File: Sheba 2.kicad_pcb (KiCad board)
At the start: 2 copper layers, 85.7 x 54 mm, 69 parts, among them J1 Conn_01x02_Pin, J2 Conn_02x04_Top_Bottom, J3 Conn_01x06_Pin, J4 Conn_01x03_Pin, J5 Conn_01x03_Pin, J6 Conn_01x03_Pin, P1 USB 2.0 Type-C Port, SW1 SPDT Switch, U1 STM32F072CBTx, U2 MIC5504-3.3YM5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

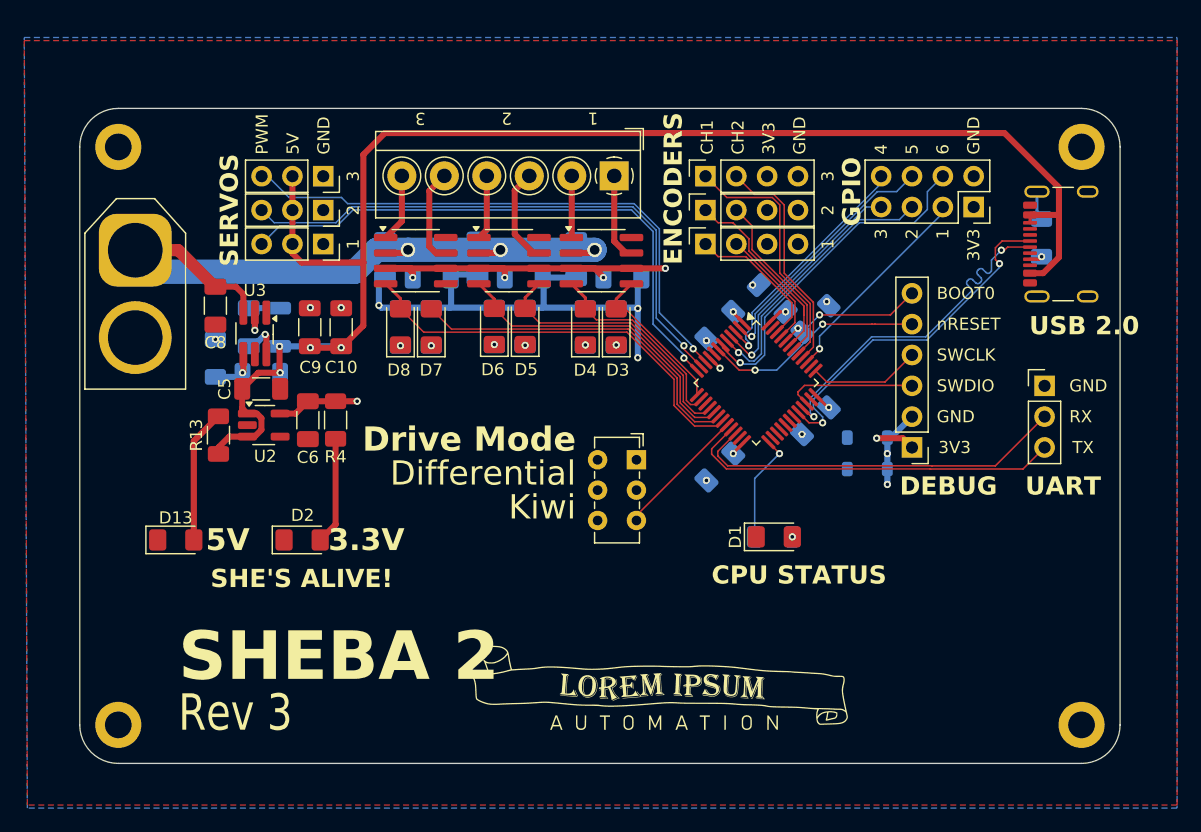
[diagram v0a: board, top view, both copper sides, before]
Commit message: change to ESP32-C6-WROOM
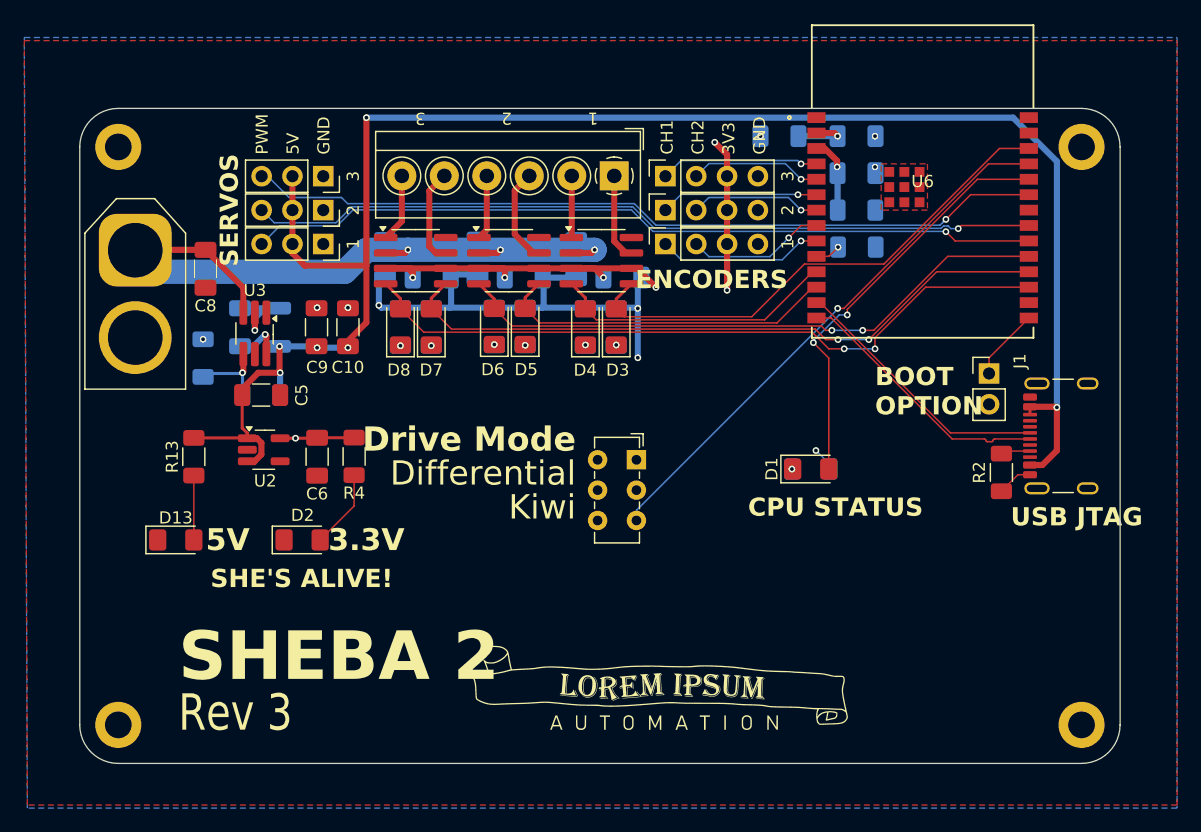
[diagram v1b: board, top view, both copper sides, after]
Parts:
- removed C4: C1uF, Capacitor_SMD:C_1206_3216Metric_Pad1.33x1.80mm_HandSolder
- removed D10, D9: D_Zener3.3V, Diode_SMD:D_SOD-123
- removed J2: Conn_02x04_Top_Bottom, Connector_PinSocket_2.54mm:PinSocket_2x04_P2.54mm_Vertical
- removed J3: Conn_01x06_Pin, Connector_PinHeader_2.54mm:PinHeader_1x06_P2.54mm_Vertical
- removed U1: STM32F072CBTx, Package_QFP:LQFP-48_7x7mm_P0.5mm
- added R14: R10k, Resistor_SMD:R_1206_3216Metric_Pad1.30x1.75mm_HandSolder, B.Cu at (117.3, 38.4)
- added U6: ESP32-C6-WROOM-1-N4, Library:MOD28_ESP32-C6-WROOM-1_EXP, F.Cu at (122.8, 36.0)
- C1: value C1uF -> C22uF
- J1: footprint Connector_PinHeader_2.54mm:PinHeader_1x03_P2.54mm_Vertical -> Connector_PinHeader_2.54mm:PinHeader_1x02_P2.54mm_Vertical
- R1: value R10k -> R220
- R2: moved to F.Cu
- R3: value R220 -> R10k
- moved C3 26.7 mm to (117.3, 35.3), turned to 180 degrees
- moved R3 24.8 mm to (117.4, 41.4), turned to 180 degrees
- moved R2 19.6 mm to (129.3, 60.0), turned to 90 degrees
- moved C2 16.3 mm to (111.0, 32.3), turned to 0 degrees
- moved P1 15.8 mm to (135.3, 57.0)
- moved C1 15.1 mm to (117.3, 32.3), turned to 180 degrees
- moved R1 12.4 mm to (113.6, 59.7), turned to 0 degrees
- moved D1 6.34 mm to (113.6, 59.7)
- moved J1 4.68 mm to (128.3, 51.8)
- moved R4 3.36 mm to (75.9, 58.6)
- moved EP2 3.30 mm to (101.6, 38.4)
- moved EP3 3.30 mm to (101.6, 35.6)
- moved EP1 3.30 mm to (101.6, 41.1)
- moved C8 3.14 mm to (63.7, 43.2)
- moved C6 3.10 mm to (72.9, 58.7)
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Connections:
- C2 pad 1: +3V3 -> GND
- C2 pad 2: GND -> +3V3
- C3 pad 2: +3V3 -> EN
- D1 pad 1: GND -> Net-(D1-K)
- D1 pad 2: Net-(D1-A) -> BLINKY
- J1 pad 1: GND -> BOOT_OPTION
- J1 pad 2: USART3_RX -> GND
- R1 pad 1: BOOT0 -> Net-(D1-K)
- R3 pad 1: BLINKY -> +3V3
- R3 pad 2: Net-(D1-A) -> Net-(U6-IO8)
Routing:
- net KIWI_DRIVE: track 10.5 -> 45.0 mm, vias 0 -> 1
- net USART3_TX: track 31.4 -> 0.00 mm
- net USART3_RX: track 31.4 -> 0.00 mm
- net M1_FWD: track 12.9 -> 42.6 mm
- net GPIO6: track 28.0 -> 0.00 mm, vias 1 -> 0
- net M3_FWD: track 29.3 -> 55.2 mm, vias 0 -> 2
- net BLINKY: track 9.03 -> 34.6 mm, vias 1 -> 2
- net M2_REV: track 25.8 -> 49.9 mm, vias 0 -> 2
- net M3_REV: track 34.6 -> 58.4 mm, vias 0 -> 2
- net GPIO2: track 23.0 -> 0.00 mm, vias 1 -> 0
- net +5V: track 123.9 -> 146.2 mm, vias 4 -> 6
- net GPIO5: track 20.9 -> 0.00 mm, vias 1 -> 0
- net GPIO4: track 20.3 -> 0.00 mm, vias 1 -> 0
- net GPIO3: track 19.7 -> 0.00 mm, vias 1 -> 0
- net SERVO1: track 47.3 -> 66.5 mm
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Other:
- board text added: "BOOT OPTION"
- board text added: "USB JTAG"
- board text removed: "4"
- board text removed: "5"
- board text removed: "6"
- board text removed: "BOOT0"
- board text removed: "DEBUG"
- board text removed: "GPIO"
- board text removed: "RX"
- board text removed: "SWCLK"
- board text removed: "SWDIO"
- board text removed: "TX"
- board text removed: "UART"
- board text removed: "USB 2.0"
- board text removed: "nRESET"
